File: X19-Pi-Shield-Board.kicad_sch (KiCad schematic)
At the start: 0 parts

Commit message: test
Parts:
- added C1, C2: 1uF, Package_SO:SOIC-8_3.9x4.9mm_P1.27mm, symbol Device:C
- added C3: 20pF, symbol Device:C
- added IC1: STM32C542CCT6, QFP50P900X900X160-48N, symbol STM32C542CCT6:STM32C542CCT6
- added U1: MIC5504-3.3YM5, Package_TO_SOT_SMD:SOT-23-5, symbol Regulator_Linear:MIC5504-3.3YM5
- added U2: BME280, Package_LGA:Bosch_LGA-8_2.5x2.5mm_P0.65mm_ClockwisePinNumbering, symbol Sensor:BME280
- added U3: INA237AIDGSR, VSSOP_IDGSR_TEX, symbol INA237AIDGSR:INA237AIDGSR
- added U4: TCAN1044VDRQ1, D0008A-IPC_A, symbol TCAN1044VDRQ1:TCAN1044VDRQ1
- added U5: MCP2518FDT-E/QBB, VDFN14_QBB_MCH, symbol MCP2518FDT_E_QBB:MCP2518FDT-E_QBB
- added Y1: ECS-120-18-33-JGN-TR, ECS-120-18-33-JGN-TR:XTAL_ECS-120-18-33-JGN-TR, symbol ECS-120-18-33-JGN-TR:ECS-120-18-33-JGN-TR
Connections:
- new net +3.3V: C2.1, C3.1, U1.5 (VOUT), Y1.1 (IN/OUT)
- new net +5V: C1.1, U1.1 (VIN)
- new net GND: C1.2, C2.2, C3.2, U1.2 (GND), Y1.2 (GND), Y1.3 (OUT/IN), Y1.4 (GND__1)
- new net MISO: IC1.27 (PB14)
- new net MOSI: IC1.28 (PB15)
- new net NRST: IC1.7 (NRST)

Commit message: finishing board stuff
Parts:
- added C4: 30pF, symbol Device:C
- added C5: 0.1uF, symbol Device:C
- added J1: Raspberry_Pi_4, symbol Connector:Raspberry_Pi_4
- added R1: 1mOhm, D0008A-IPC_A, symbol Device:R_Small_US
- added R2, R3, R4: 4.7k, symbol Device:R_Small_US
- added U6: TCAN1044VDRQ1, D0008A-IPC_A, symbol TCAN1044VDRQ1:TCAN1044VDRQ1
- C3: value 20pF -> 30pF
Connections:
- net +3.3V: now also U4.5 (VIO), U6.5 (VIO)
- net +5V: now also U1.3 (EN), U3.6 (VS), U3.8 (VBUS), U3.9 (IN-), U4.3 (VCC), C5.1, R1.2, R2.1, R3.1, R4.1, U6.3 (VCC)
- net GND: now also U2.1 (GND), U2.7 (GND), U3.1 (A1), U3.2 (A0), U3.7 (GND), U4.2 (GND), C4.2, C5.2, U6.2 (GND); no longer Y1.3 (OUT/IN)
- net MISO: now also U5.12 (SDO), J1.35 (GPIO19/SPI1_MISO/PCM_FS); no longer IC1.27 (PB14)
- net MOSI: now also U5.11 (SDI), J1.38 (GPIO20/SPI1_MOSI/PCM_DIN/PWM1); no longer IC1.28 (PB15)
- net TXD: now reaches IC1.2 (PC13)
- net TXD: now also U4.1 (TXD), U5.1 (TXCAN), J1.8 (GPIO14/UART_TXD)
- net RXD: now reaches IC1.3 (PC14-OSC32_IN)
- net RXD: now also U4.4 (RXD), U5.2 (RXCAN), J1.10 (GPIO15/UART_RXD)
- net OSC_IN: now reaches IC1.5 (PH0-OSC_IN)
- net OSC_IN: now also U5.6 (OSC1)
- net OSC_OUT: now reaches IC1.6 (PH1-OSC_OUT)
- net OSC_OUT: now also U5.5 (OSC2)
- net Vin: now reaches U3.10 (IN+)
- net Vin: now also R1.1
- net GPIO: now reaches U3.3 (ALERT)
- net GPIO: now also R4.2
- net I2C SDA: now reaches U3.4 (SDA)
- net I2C SDA: now also J1.27 (ID_SD_I2C0/GPIO00), R3.2
- net I2C SCL: now reaches U3.5 (SCL)
- net I2C SCL: now also J1.28 (ID_SC_I2C0/GPIO01), R2.2
- net SCLK: now reaches U5.10 (SCK)
- net SCLK: now also J1.40 (GPIO21/SPI1_SCLK/PCM_DOUT)
- net CS: now reaches U5.13 (nCS)
- net CS: now also J1.12 (GPIO18/SPI1_~{CE0}/PCM_CLK/PWM0)
- net STBY: now reaches U5.9 (*INT0/GPIO0/XSTBY)
- net STBY: now also U4.8 (STB)
- net CANL: now reaches U4.6 (CANL)
- net CAN+: now reaches U4.7 (CANH)
- net CAN+: now also U6.7 (CANH)
- new net: C4.1, Y1.3 (OUT/IN)
- new net: J1.1 (3V3), J1.17 (3V3)
- new net: J1.14 (GND), J1.20 (GND), J1.25 (GND), J1.30 (GND), J1.34 (GND), J1.39 (GND), J1.6 (GND), J1.9 (GND)
- new net: J1.2 (5V), J1.4 (5V)
- new net CAN-: U6.6 (CANL)
- new net RXDSTM: U6.4 (RXD)
- new net STBYSTM: U6.8 (STB)
- new net TXDSTM: U6.1 (TXD)
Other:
- moved on the sheet: C1, C2, C3, IC1, U1, U4, U5, Y1

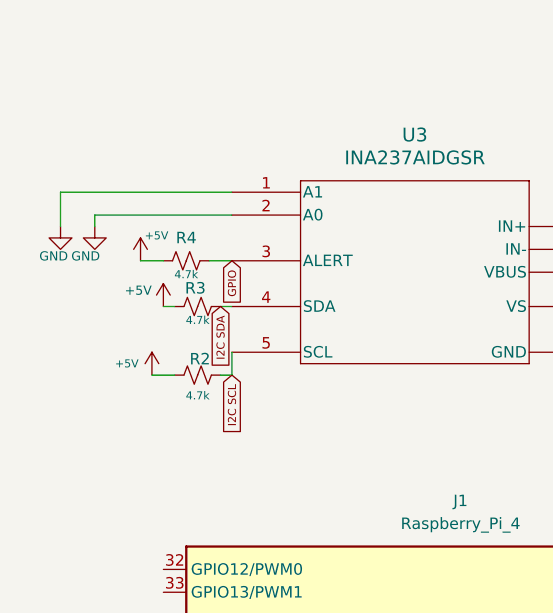
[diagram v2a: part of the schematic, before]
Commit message: adjust schematic and add board outline on pcb
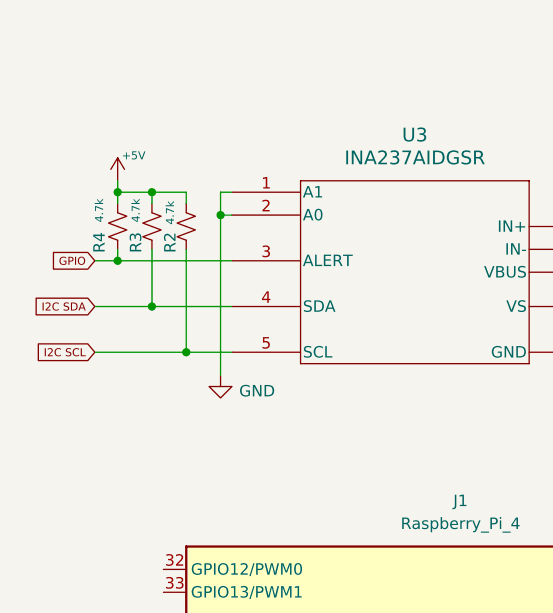
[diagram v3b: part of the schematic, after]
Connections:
- net +5V: now also R2.2, R3.2, R4.2; no longer R2.1, R3.1, R4.1
- net GPIO: now also R4.1; no longer R4.2
- net I2C SCL: now also R2.1; no longer R2.2
- net I2C SDA: now also R3.1; no longer R3.2
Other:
- moved on the sheet: R3

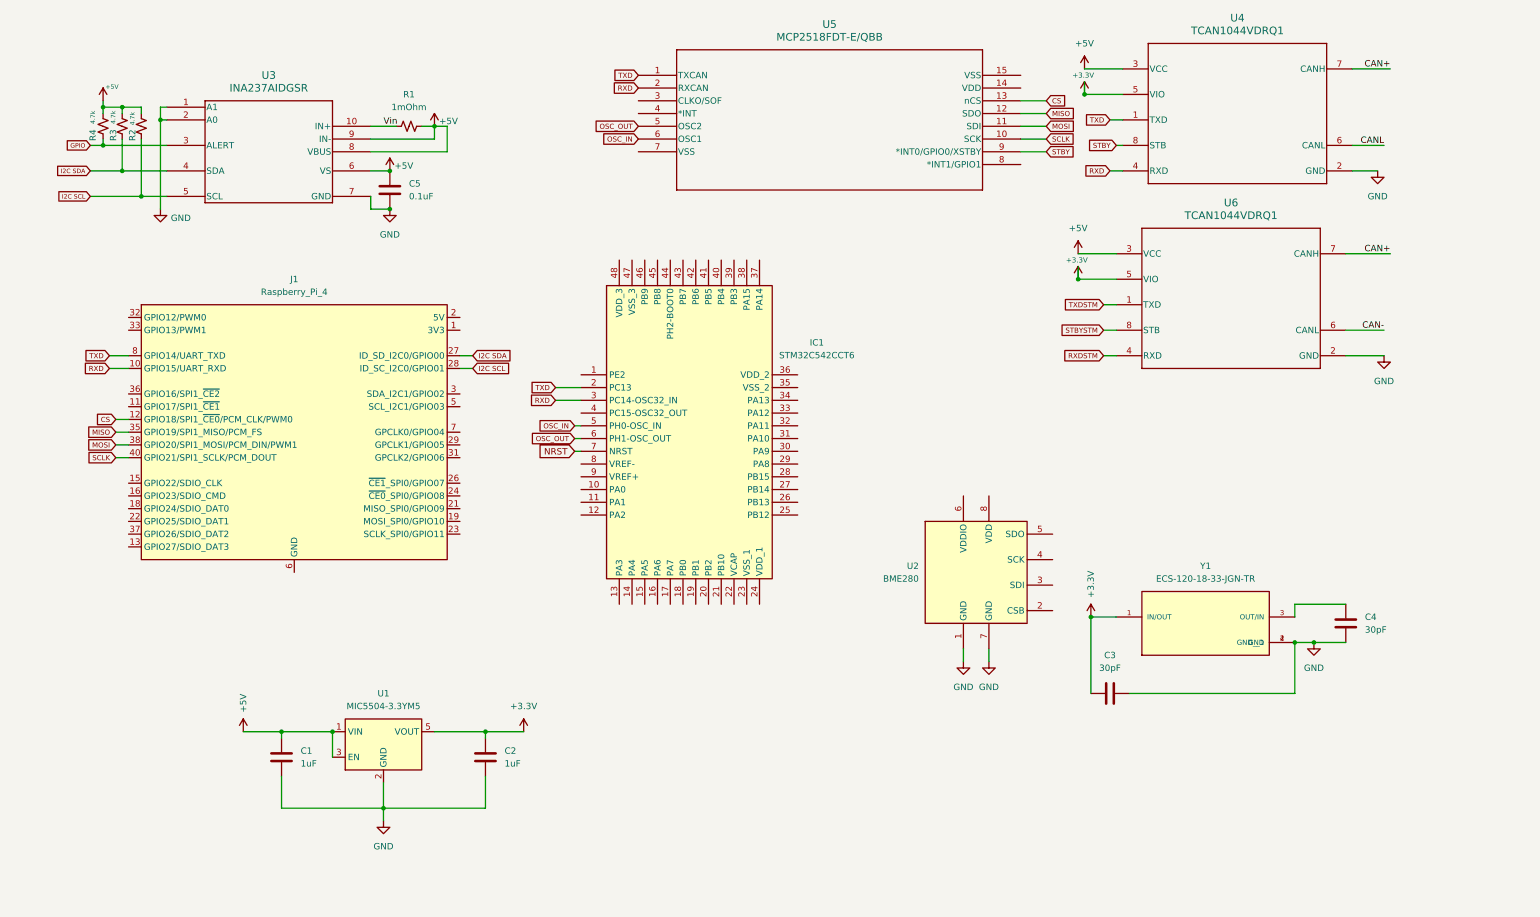
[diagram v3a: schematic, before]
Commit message: add connectors, mounting holes, fix some stuff
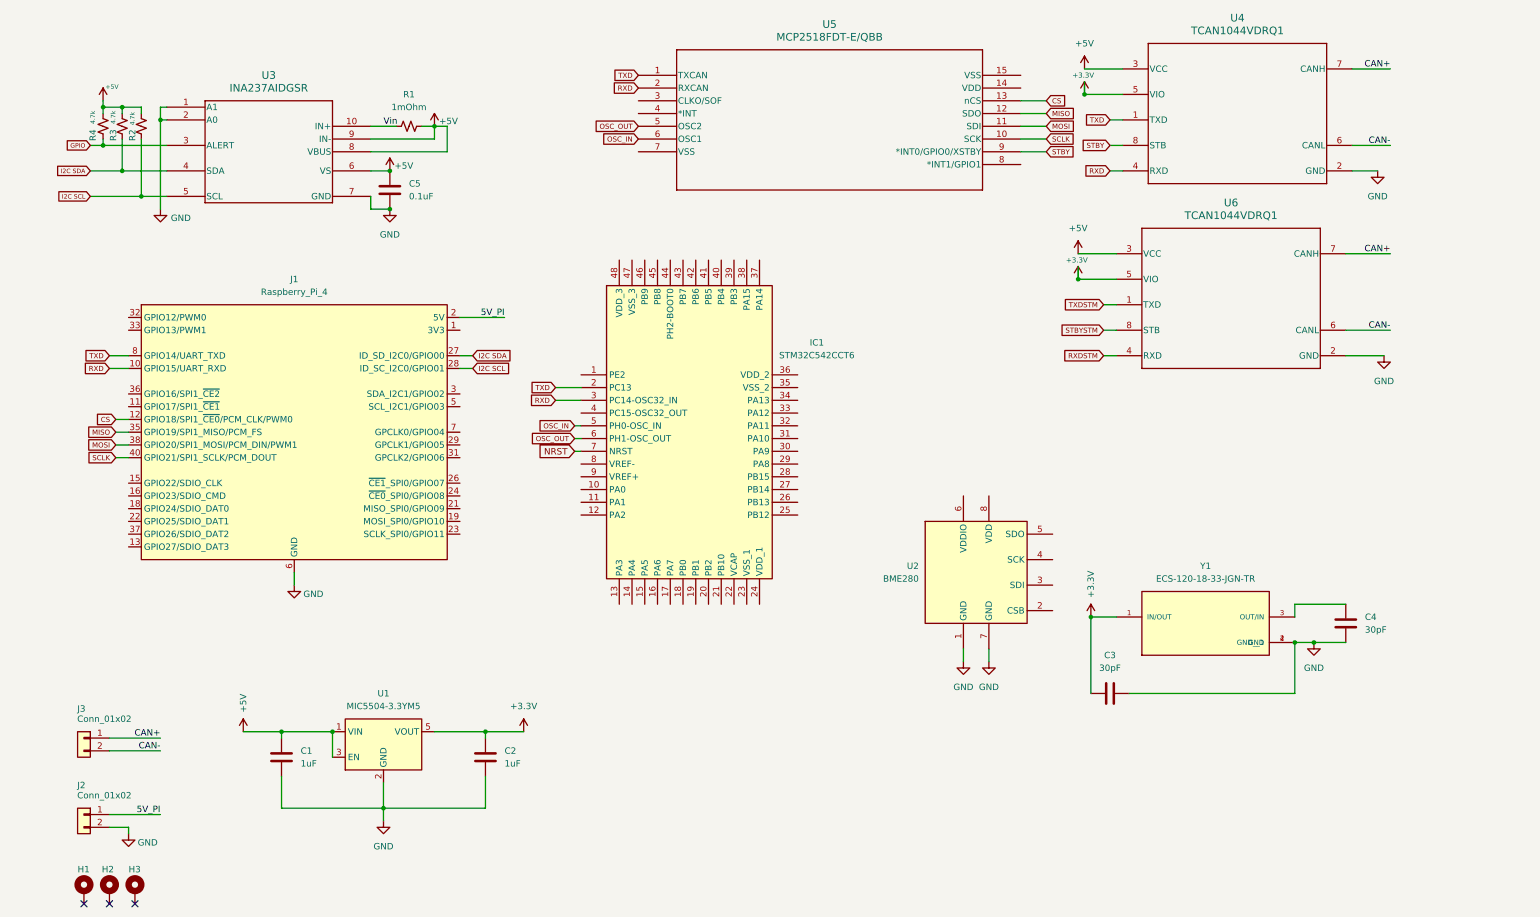
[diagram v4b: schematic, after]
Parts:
- added H1, H2, H3: MountingHole_Pad, symbol Mechanical:MountingHole_Pad
- added J2, J3: Conn_01x02, rov_connectors:0436500200, symbol Connector_Generic:Conn_01x02
- J1: footprint (none) -> Connector_PinSocket_2.54mm:PinSocket_2x20_P2.54mm_Vertical
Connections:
- net CANL is gone; now on net CAN-: U4.6 (CANL)
- net CAN+: now also J3.1 (Pin_1)
- net CAN-: now also J3.2 (Pin_2)
- net GND: now also J1.14 (GND), J1.20 (GND), J1.25 (GND), J1.30 (GND), J1.34 (GND), J1.39 (GND), J1.6 (GND), J1.9 (GND), J2.2 (Pin_2)
- net 5V_PI: now reaches J1.2 (5V), J1.4 (5V)
- net 5V_PI: now also J2.1 (Pin_1)
- no-connect marks 0 -> 3

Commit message: changes pre STM
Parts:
- added C10, C9: 100n, symbol Device:C
- added C6: 0.1u, symbol Device:C
- added C7, C8: 22p, symbol Device:C
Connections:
- net +3.3V: now also U2.6 (VDDIO), U5.14 (VDD), C6.1, C9.1
- net +5V: now also U2.8 (VDD), C10.2
- net CS: now also U2.2 (CSB)
- net GND: now also U5.15 (VSS), U5.7 (VSS), C10.1, C6.2, C7.1, C8.1; no longer U2.7 (GND)
- net MISO: now also U2.5 (SDO)
- net MOSI: now also U2.3 (SDI)
- net OSC_IN: now also U5.3 (CLKO/SOF), C7.2
- net OSC_OUT: now also C8.2
- net RXD: no longer IC1.3 (PC14-OSC32_IN)
- net RXDSTM: now also IC1.3 (PC14-OSC32_IN)
- net SCLK: now also U2.4 (SCK)
- net STBY: now also J1.13 (GPIO27/SDIO_DAT3)
- net STBYSTM: now also IC1.10 (PA0)
- net TXD: no longer IC1.2 (PC13)
- net TXDSTM: now also IC1.2 (PC13)
- net INT_PI: now reaches U5.4 (*INT)
- net INT_PI: now also J1.22 (GPIO25/SDIO_DAT1)
- net 3.3VLDO: now reaches J1.1 (3V3), J1.17 (3V3)
- new net: C9.2, U2.7 (GND)
- no-connect marks 3 -> 4
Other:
- moved on the sheet: IC1, U2, U5

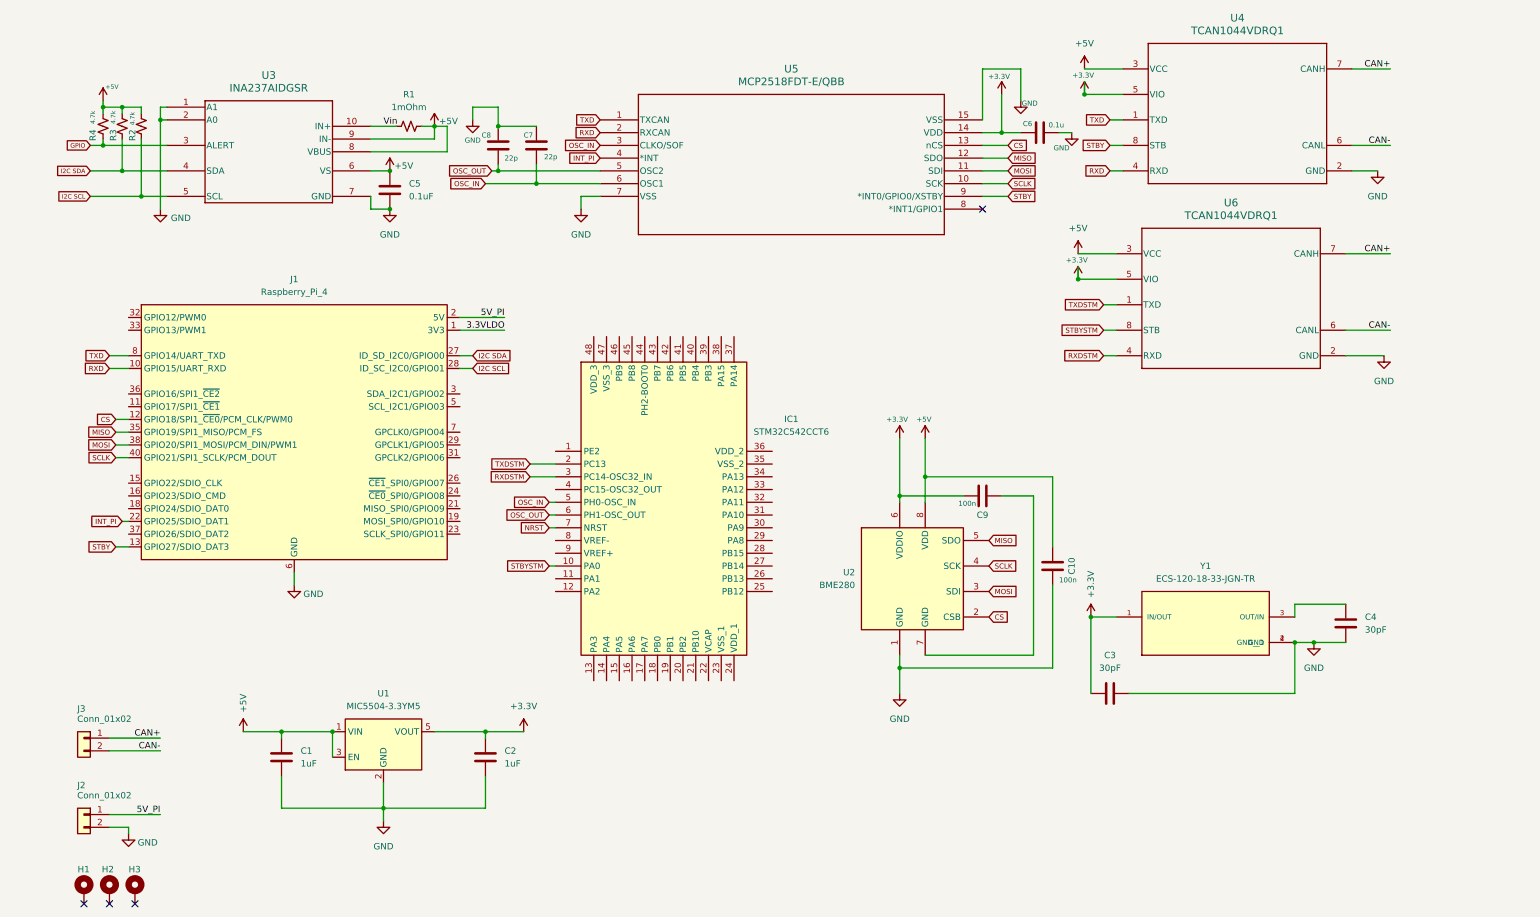
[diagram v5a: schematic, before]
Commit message: Initial Feedback - oscillator, unwired capacitors, general moving stuff around
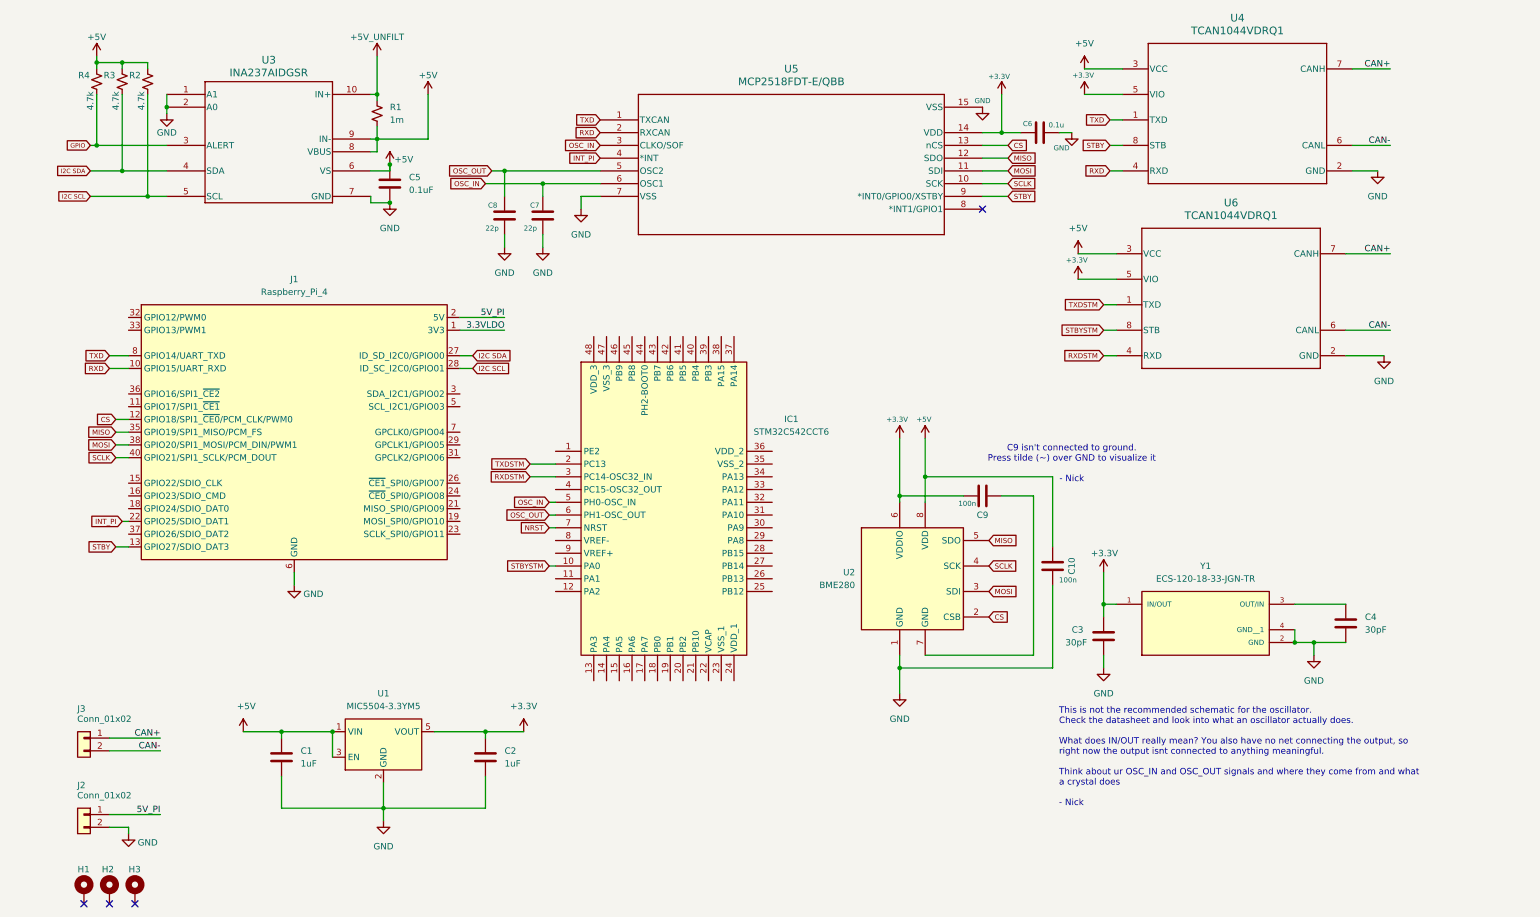
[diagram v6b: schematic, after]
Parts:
- R1: value 1mOhm -> 1m
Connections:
- net GND: now also C7.2, C8.2; no longer C7.1, C8.1
- net OSC_IN: now also C7.1; no longer C7.2
- net OSC_OUT: now also C8.1; no longer C8.2
- net Vin renamed +5V_UNFILT
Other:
- note added: "C9 isn't connected to ground. Press tilde (~) over GND to visualize it - Nick"
- note added: "This is not the recommended schematic for the oscillator. Check the datasheet and look into what an oscillator actually does. What does IN/OUT really mean? You also have no net connecting the output, so right now the output isnt connected to anything meaningful. Think about ur OSC_IN and OSC_OUT signals and where they come from and what a crystal does - Nick"
- moved on the sheet: C3, C5, C7, C8, R1, R2, R3, R4, U3

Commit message: add sam feedback
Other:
- note added: "consider also 1uF decoupling for this IC might have some spiky power draw due to CAN could also mirror the schematic and connect TXD and RXD to the transciever directly"
- note added: "make sure your power input to this IC is connected to the connector power input (J2) right now, +5V_UNFILT is on a different net than 5V_PI, the connector 5V net"
- note added: "these GND nets are not connected pin 7 is not grounded"
- note added: "think about these 5v net connections, if we want to measure the current the Pi is drawing, we can't connect the connector's 5V input (J2 pin 1) and the pi's 5V pin directly (J1 pin 2), or there will be nowhere to put the 1mOhm resistor to measure the drop"
- note added: "your power and gnd are not connected on the STM, also no decoupling caps"
- moved on the sheet: C1, C2, R1, U1
